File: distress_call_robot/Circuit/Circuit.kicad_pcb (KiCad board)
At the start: 2 copper layers, 6 parts, among them M1 JST-2p, M2 JST-2p, U1 L293D

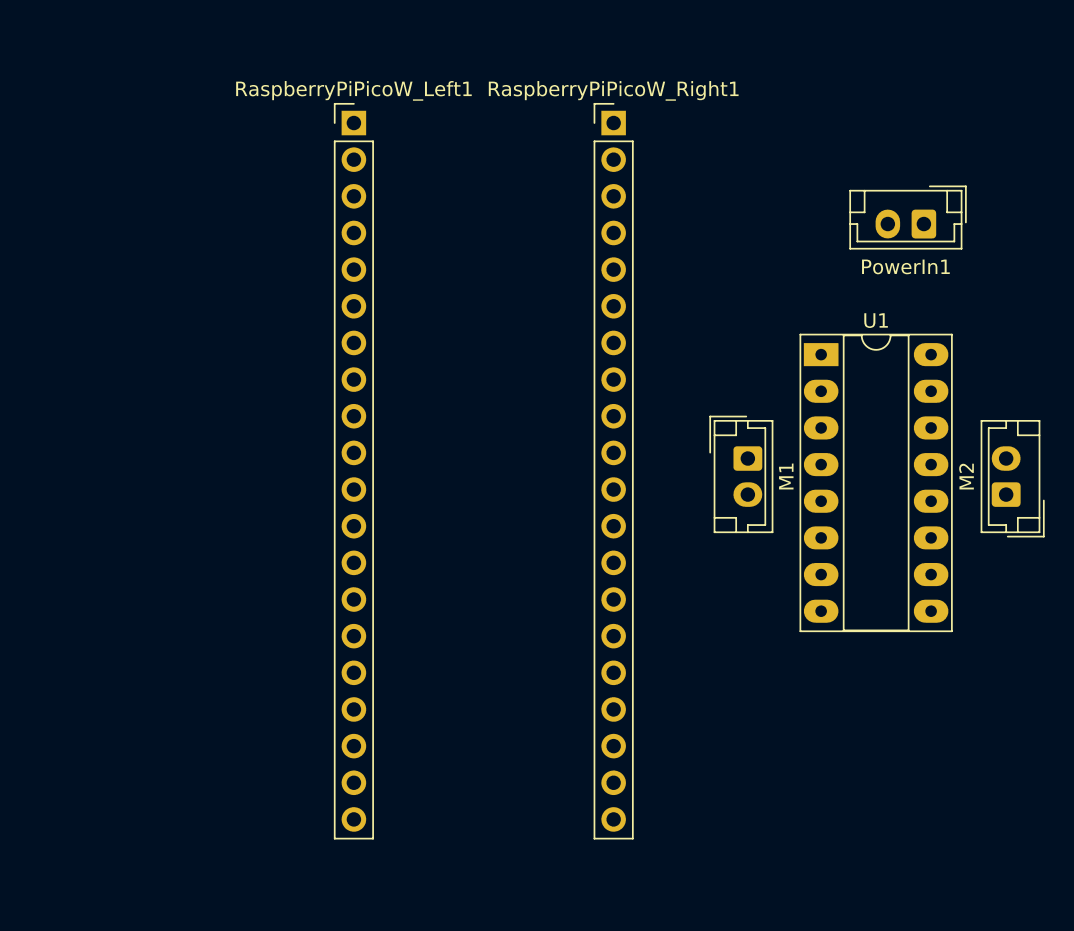
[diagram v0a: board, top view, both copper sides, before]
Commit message: finished distress robot PCB and DC motor differential control code
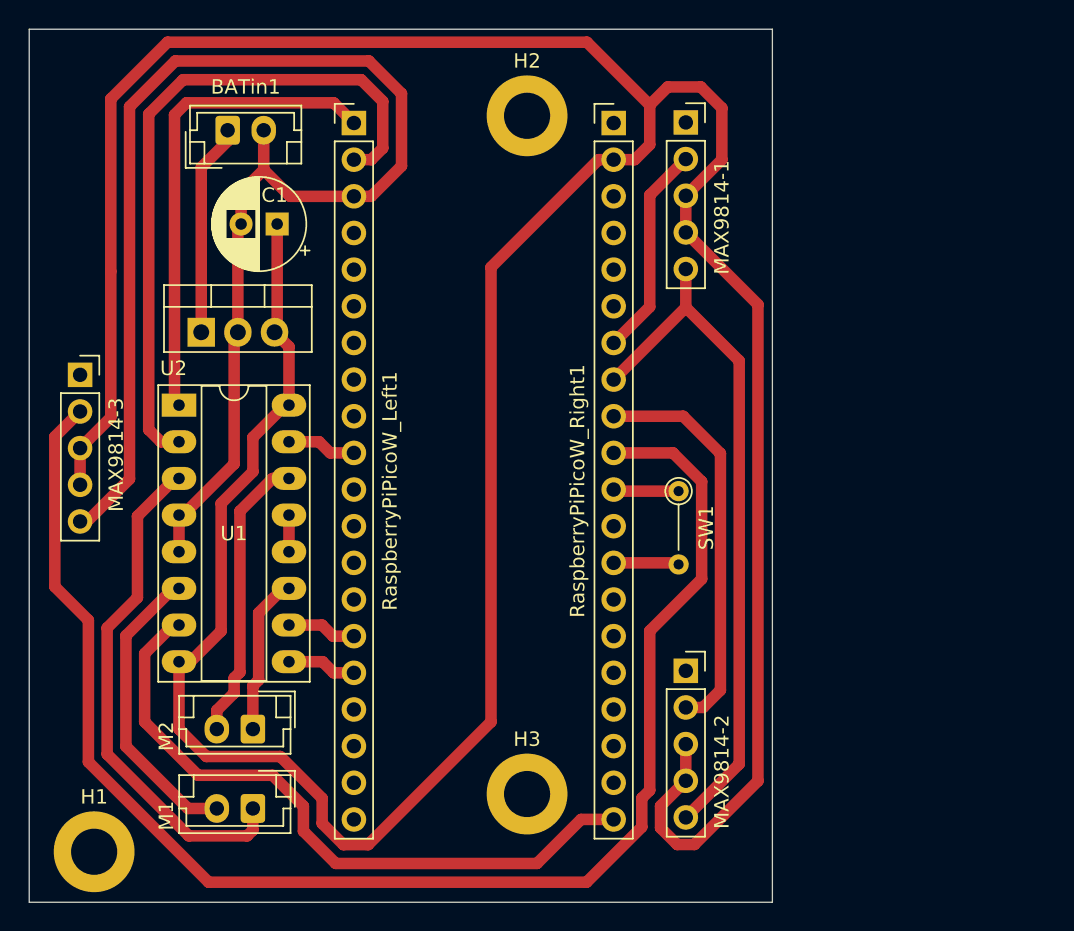
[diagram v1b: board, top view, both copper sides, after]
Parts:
- added C1: 330uF, Capacitor_THT:CP_Radial_D6.3mm_P2.50mm, F.Cu at (136.7, 77.0)
- added H1: MountingHole, MountingHole:MountingHole_3.2mm_M3_DIN965_Pad, F.Cu at (124.0, 120.5)
- added H2: MountingHole, MountingHole:MountingHole_3.2mm_M3_DIN965_Pad, F.Cu at (154.0, 69.5)
- added H3: MountingHole, MountingHole:MountingHole_3.2mm_M3_DIN965_Pad, F.Cu at (154.0, 116.5)
- added MAX9814-1: Conn_01x05, Connector_PinSocket_2.54mm:PinSocket_1x05_P2.54mm_Vertical, F.Cu at (165.0, 70.0)
- added MAX9814-2: Conn_01x05, Connector_PinSocket_2.54mm:PinSocket_1x05_P2.54mm_Vertical, F.Cu at (165.0, 108.0)
- added MAX9814-3: Conn_01x05, Connector_PinSocket_2.54mm:PinSocket_1x05_P2.54mm_Vertical, F.Cu at (123.0, 87.5)
- added SW1: SW_Push, Resistor_THT:R_Axial_DIN0204_L3.6mm_D1.6mm_P5.08mm_Vertical, F.Cu at (164.5, 95.5)
- added U2: L7805, Package_TO_SOT_THT:TO-220-3_Vertical, F.Cu at (131.4, 84.5)
- BATin1: renamed from PowerIn1; value JST-2p -> JST2P
- M1, M2: value JST-2p -> JST2P
- moved M2 54.7 mm to (135.0, 112.0), turned to 180 degrees
- moved BATin1 48.7 mm to (133.2, 70.5), turned to 0 degrees
- moved U1 44.6 mm to (129.9, 89.5)
- moved M1 42.0 mm to (135.0, 117.5), turned to 180 degrees
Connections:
- BATin1 pad 1: +5V -> +8V
- RaspberryPiPicoW_Left1 pad 1: unconnected-(RaspberryPiPicoW_Left1-Pin_1-Pad1) -> EN1
- RaspberryPiPicoW_Left1 pad 10: unconnected-(RaspberryPiPicoW_Left1-Pin_10-Pad10) -> IN2B
- RaspberryPiPicoW_Left1 pad 15: unconnected-(RaspberryPiPicoW_Left1-Pin_15-Pad15) -> IN2A
- RaspberryPiPicoW_Left1 pad 16: unconnected-(RaspberryPiPicoW_Left1-Pin_16-Pad16) -> EN2
- RaspberryPiPicoW_Left1 pad 2: unconnected-(RaspberryPiPicoW_Left1-Pin_2-Pad2) -> IN1A
- RaspberryPiPicoW_Left1 pad 3: unconnected-(RaspberryPiPicoW_Left1-Pin_3-Pad3) -> GND
- RaspberryPiPicoW_Right1 pad 10: unconnected-(RaspberryPiPicoW_Right1-Pin_10-Pad10) -> ADC1
- RaspberryPiPicoW_Right1 pad 11: unconnected-(RaspberryPiPicoW_Right1-Pin_11-Pad11) -> RUN
- RaspberryPiPicoW_Right1 pad 13: unconnected-(RaspberryPiPicoW_Right1-Pin_13-Pad13) -> RUN_GND
- RaspberryPiPicoW_Right1 pad 2: unconnected-(RaspberryPiPicoW_Right1-Pin_2-Pad2) -> VSYS
- RaspberryPiPicoW_Right1 pad 20: unconnected-(RaspberryPiPicoW_Right1-Pin_20-Pad20) -> IN1B
- RaspberryPiPicoW_Right1 pad 7: unconnected-(RaspberryPiPicoW_Right1-Pin_7-Pad7) -> ADC3
- RaspberryPiPicoW_Right1 pad 8: unconnected-(RaspberryPiPicoW_Right1-Pin_8-Pad8) -> ADCGND
- RaspberryPiPicoW_Right1 pad 9: unconnected-(RaspberryPiPicoW_Right1-Pin_9-Pad9) -> ADC2
- U1 pad 12: unconnected-(U1-GND-Pad12) -> Net-(U1-GND-Pad12)
- U1 pad 13: unconnected-(U1-GND-Pad13) -> Net-(U1-GND-Pad12)
- U1 pad 16: +5V -> VSYS
- U1 pad 4: unconnected-(U1-GND-Pad4) -> GND
- U1 pad 5: unconnected-(U1-GND-Pad5) -> GND
- U1 pad 8: +5V -> VSYS
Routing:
- net VSYS: track 0.00 -> 257.4 mm
- net ADC1: track 0.00 -> 101.9 mm
- net GND: track 0.00 -> 99.5 mm
- net ADCGND: track 0.00 -> 48.2 mm
- net IN1A: track 0.00 -> 47.7 mm
- net IN1B: track 0.00 -> 46.8 mm
- net Net-(M1-+): track 0.00 -> 35.7 mm
- net EN1: track 0.00 -> 33.6 mm
- net ADC2: track 0.00 -> 27.8 mm
- net Net-(M1--): track 0.00 -> 21.2 mm
- net Net-(M2--): track 0.00 -> 20.5 mm
- net ADC3: track 0.00 -> 14.8 mm
- net +8V: track 0.00 -> 14.8 mm
- net Net-(M2-+): track 0.00 -> 11.3 mm
- net EN2: track 0.00 -> 4.82 mm
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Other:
- board outline added: 51.5 x 60.5 mm
